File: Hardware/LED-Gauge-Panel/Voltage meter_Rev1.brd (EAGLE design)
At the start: 34.3 x 58.4 mm, 31 parts, among them J3 SL04, Q4 MOSFET-NCHANNEL2N7002PW, Q5 MOSFET-NCHANNEL2N7002PW, Q6 MOSFET-NCHANNEL2N7002PW, U1 ATMEGA328P_PDIP, U21 MAX232D, X1 22-23-2031, X2 16MHz

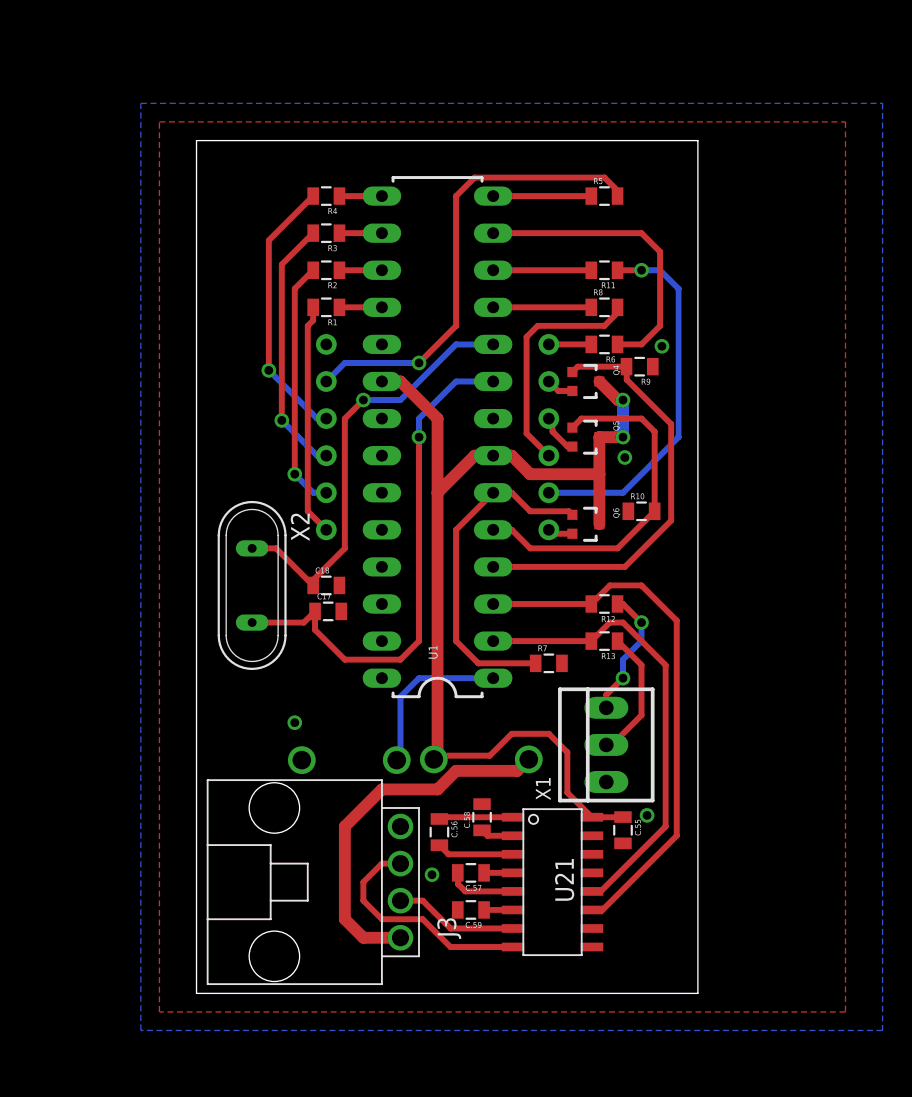
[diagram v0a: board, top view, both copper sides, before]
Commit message: Review 2 changes
Changed from n channel mosfets to p channel. Removed the resistors on
the control lines to the mosfets.
moved the resistors in series with the programming pins. And put
capacitors in the VCC lines.
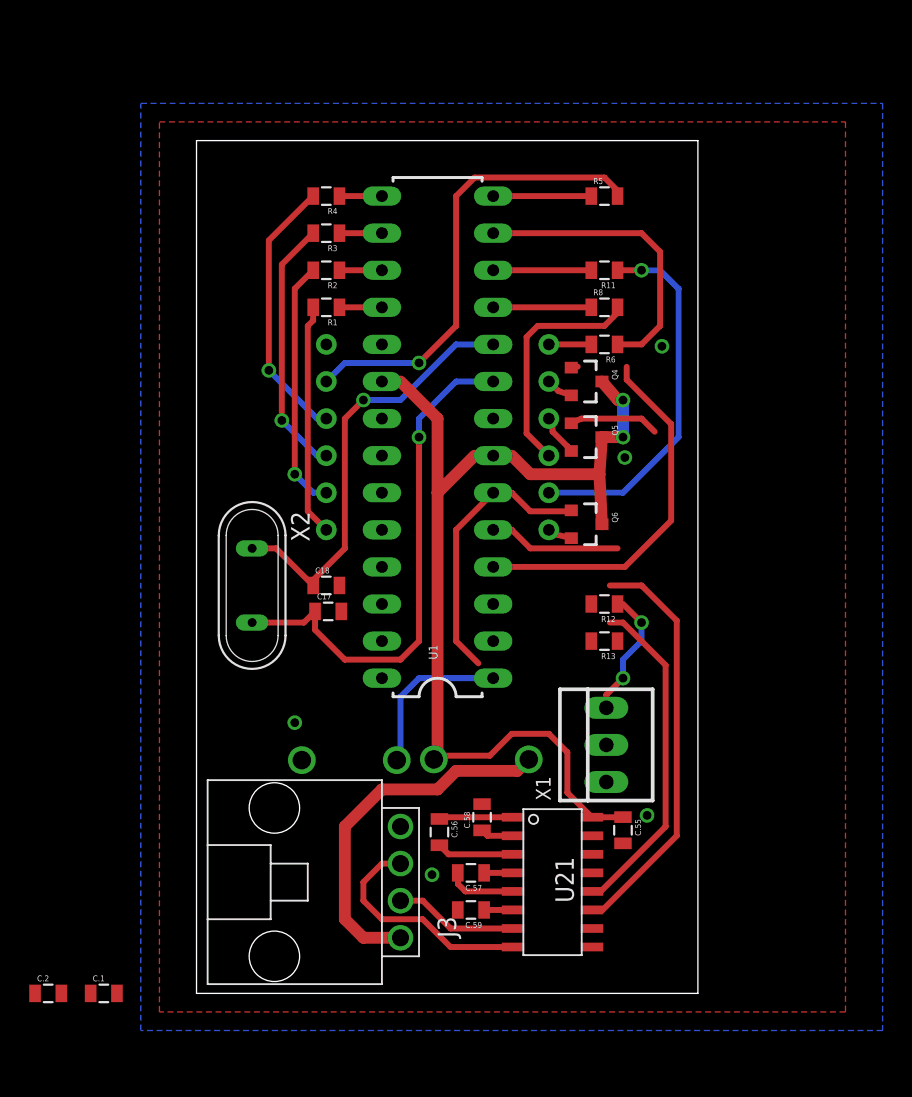
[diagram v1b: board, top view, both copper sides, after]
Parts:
- removed R10, R7, R9: 100k, SparkFun-Passives:0805
- added C.1, C.2: .1u, SparkFun-Passives:0805
- Q4, Q5, Q6: value MOSFET-NCHANNEL2N7002PW -> MOSFET-PCHANNEL; device SparkFun-DiscreteSemi:SOT323 -> SparkFun-DiscreteSemi:SOT23-3
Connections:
- new net N$15: C.2.1, U1.7
- new net N$16: C.1.1, U1.20
- net 5V: now also C.1.2, C.2.2; no longer U1.20, U1.7
- net GND: no longer R10.1, R7.2, R9.1
- net N$12: now also R13.2; no longer R13.1
- net N$14: now also R12.2; no longer R12.1
- net Q4: no longer R9.2
- net Q5: no longer R10.2
- net Q6: no longer R7.1
- net SER_RX: now also R13.1; no longer R13.2
- net SER_TX: now also R12.1; no longer R12.2
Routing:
- net Q5: track 24.4 -> 15.2 mm
- net N$12: track 9.01 -> 0.00 mm
- net SER_TX: track 36.7 -> 28.2 mm
- net SER_RX: track 31.5 -> 23.0 mm
- net 5V: track 70.5 -> 66.5 mm
- net Q6: track 23.3 -> 19.3 mm
- net Q4: track 29.2 -> 25.7 mm

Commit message: Modifications from second review
The atmega chip was changed to be surface mount. Wires were rerouted and
DRC was run. Capacitors added as well.
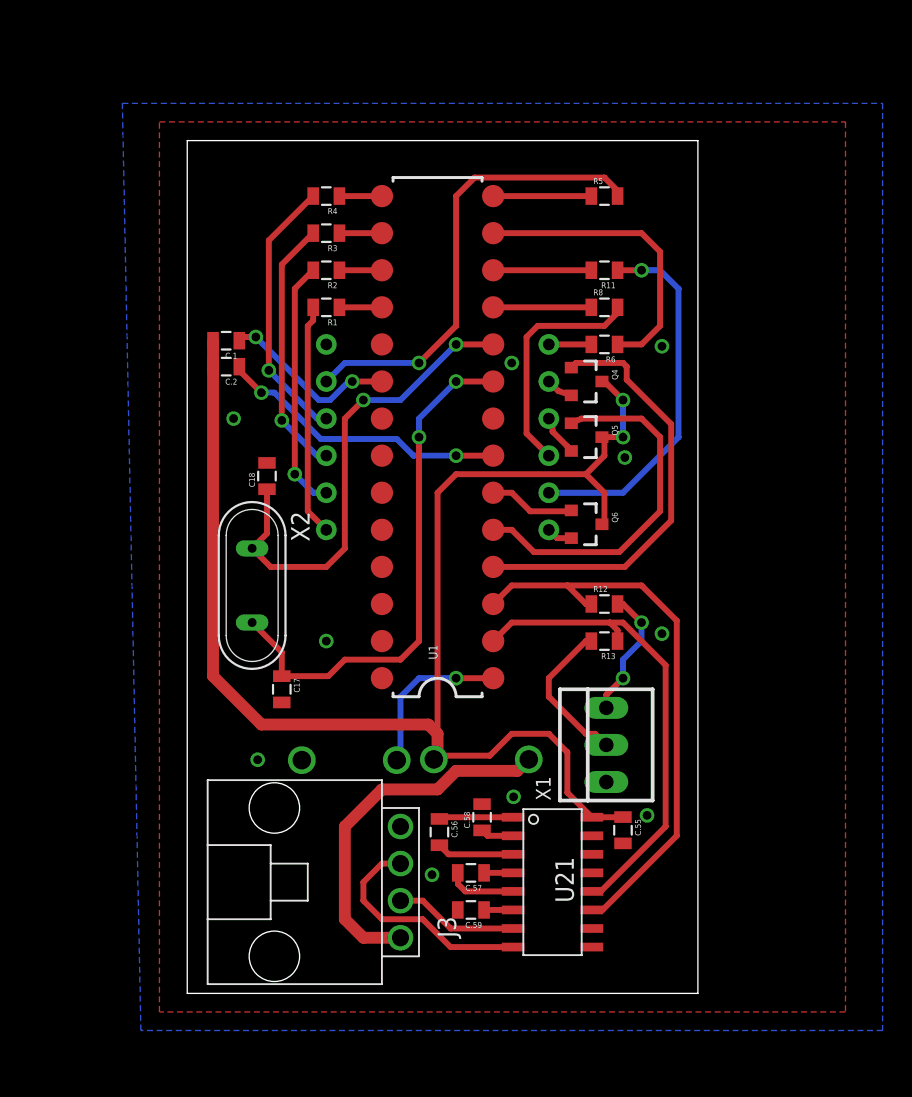
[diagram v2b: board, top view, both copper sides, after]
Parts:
- U1: value ATMEGA328P_PDIP -> ATMEGA328P_PDIPDIL28-4; device SparkFun-DigitalIC:DIL28-3 -> SparkFun-DigitalIC:CONN_IC_DIP_SOCKET_28POS
- moved C.1 45.5 mm to (4.57, 46.0), turned to 180 degrees
- moved C.2 44.6 mm to (4.57, 44.2), turned to 180 degrees
- moved C18 8.52 mm to (7.37, 36.7), turned to 90 degrees
- moved C17 6.21 mm to (8.38, 22.1), turned to 270 degrees
- moved U1 1.27 mm to (19.1, 40.6)
- turned R12 to 0 degrees
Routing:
- net 5V: track 66.5 -> 99.5 mm
- net N$15: track 0.00 -> 20.1 mm, vias 0 -> 2
- net Q6: track 19.3 -> 5.89 mm
- net N$16: track 0.00 -> 12.2 mm, vias 0 -> 2
- net SER_TX: track 28.2 -> 38.9 mm
- net N$12: track 0.00 -> 10.5 mm
- net SER_RX: track 23.0 -> 33.0 mm
- net Q5: track 15.2 -> 25.0 mm
- net Q4: track 25.7 -> 29.3 mm
- net N$51: track 29.8 -> 33.0 mm, vias 1 -> 2
- net N$50: track 35.7 -> 36.3 mm, vias 1 -> 2
- net N$13: vias 0 -> 1
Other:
- board size 34.3 x 58.4 mm -> 35 x 58.4 mm

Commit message: Reroute and label
Minor changes made to the positioning of the capacitors. Some traces
were changed due to the capacitor changes and some changes were made to
keep the trace from jumping between levels. Labels were positioned on
the board and MRDT symbol was placed on the board as well as a brief
board discription.
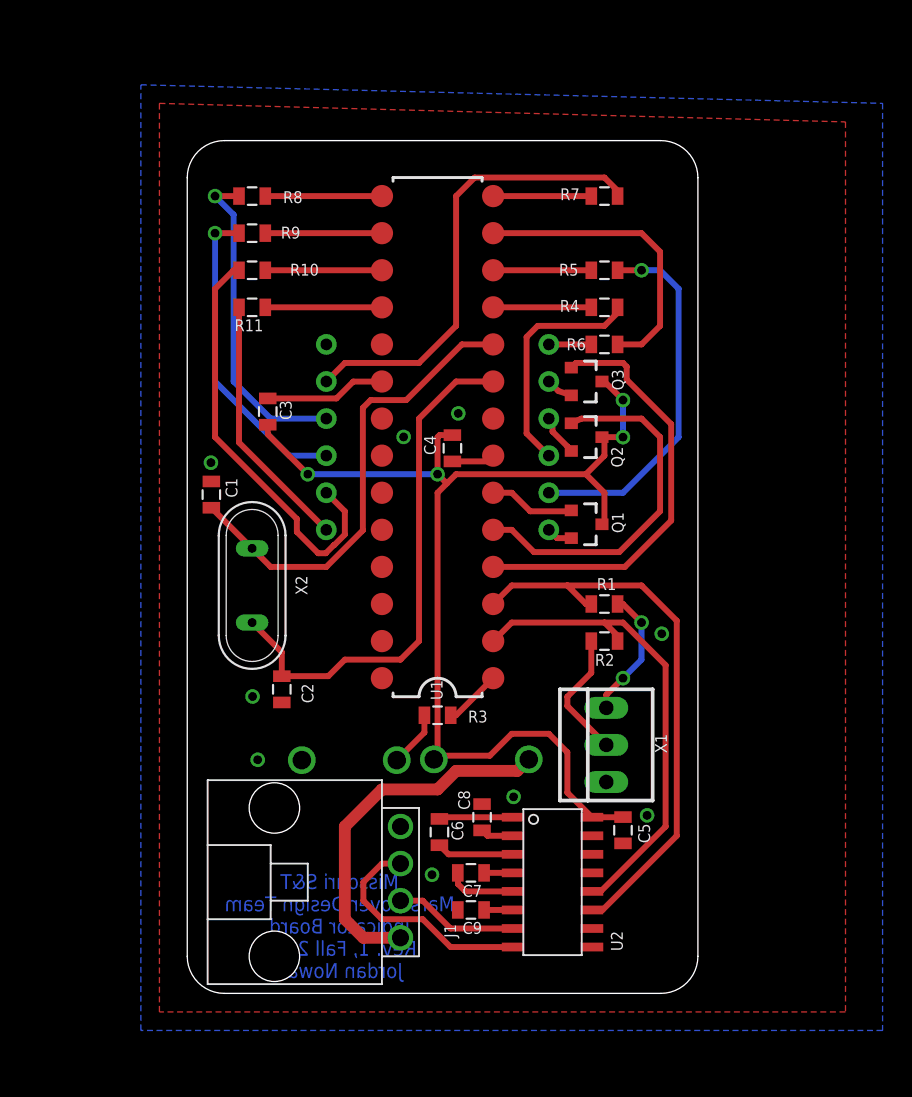
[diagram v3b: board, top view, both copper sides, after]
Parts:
- removed C.1, C.2: .1u, SparkFun-Passives:0805
- removed C18: 22pf, SparkFun-Passives:0805
- removed R12, R13: 1k, SparkFun-Passives:0805
- added C1: 22pf, SparkFun-Passives:0805
- added C3, C4: .1u, SparkFun-Passives:0805
- added LOGO1: MRDT_LOGO, MRDT-Hardware:MRDT_LOGO
- added R10, R7, R9: 330, SparkFun-Passives:0805
- R1, R2, R3: value 330 -> 1k
- moved R3 33.9 mm to (19.1, 20.3)
- moved R2 31.8 mm to (30.5, 25.4)
- moved R1 27.9 mm to (30.5, 27.9), turned to 0 degrees
- moved R8 25.3 mm to (6.35, 55.9), turned to 180 degrees
- moved R11 24.3 mm to (6.35, 48.3)
- moved R4 20.5 mm to (30.5, 48.3), turned to 0 degrees
- moved R5 5.08 mm to (30.5, 50.8), turned to 180 degrees
- moved S1 4.68 mm to (16.0, 15.5), turned to 0 degrees
- moved S2 4.68 mm to (19.1, 19.1), turned to 180 degrees
- renumbered C.55 to C5, C.56 to C6, C.57 to C7, C.58 to C8, C.59 to C9, C17 to C2, J3 to J1, Q4 to Q3, Q5 to Q2, Q6 to Q1, U21 to U2
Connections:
- new net N$24: R3.1, U1.1
- net 5V: now also C3.2, C4.2, S2.P$1; no longer C.1.2, C.2.2, S1.P$1
- net A: now also R5.1; no longer R11.1
- net C: now also R8.2; no longer R4.2
- net D: now also R10.2; no longer R2.2
- net DP: now also R9.2; no longer R3.2
- net E: now also R11.2; no longer R1.2
- net F: now also R4.2; no longer R8.2
- net G: now also R7.2; no longer R5.2
- net GND: now also C1.2, S1.P$2; no longer C18.2, S2.P$2
- net N$1: now also R7.1; no longer R5.1
- net N$10: now also R11.1; no longer R1.1
- net N$12: now also R2.2; no longer R13.2
- net N$13: now also R3.2, S1.P$1; no longer S2.P$1, U1.1
- net N$14: now also R1.2; no longer R12.2
- net N$15: now also C4.1; no longer C.2.1
- net N$16: now also C3.1; no longer C.1.1
- net N$20: now also R4.1; no longer R8.1
- net N$5: now also R8.1; no longer R4.1
- net N$51: now also C1.1; no longer C18.1
- net N$6: now also R9.1; no longer R3.1
- net N$7: now also S2.P$2; no longer S1.P$2
- net N$8: now also R5.2; no longer R11.2
- net N$9: now also R10.1; no longer R2.1
- net SER_RX: now also R2.1; no longer R13.1
- net SER_TX: now also R1.1; no longer R12.1
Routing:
- net 5V: track 99.5 -> 77.4 mm, vias 2 -> 4
- net N$15: track 20.1 -> 2.96 mm, vias 2 -> 0
- net D: track 17.2 -> 28.9 mm, vias 1 -> 0
- net N$13: track 11.3 -> 3.86 mm, vias 1 -> 0
- net N$9: track 2.91 -> 7.99 mm
- net N$6: track 2.91 -> 7.99 mm
- net N$5: track 2.91 -> 7.99 mm
- net N$10: track 2.91 -> 7.99 mm
- net N$24: track 0.00 -> 3.96 mm
- net N$16: track 12.2 -> 8.30 mm, vias 2 -> 0
- net C: track 18.5 -> 22.3 mm
- net DP: track 17.8 -> 21.5 mm
- net E: track 15.9 -> 17.7 mm
- net N$12: track 10.5 -> 8.90 mm
- net N$51: track 33.0 -> 32.2 mm, vias 2 -> 0
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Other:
- outline, holes or cut-outs redrawn
- board text added: "Missouri S&T Mars Rover Design Team Indicator Board Rev. 1, Fall 2016 Jordan Nowak"

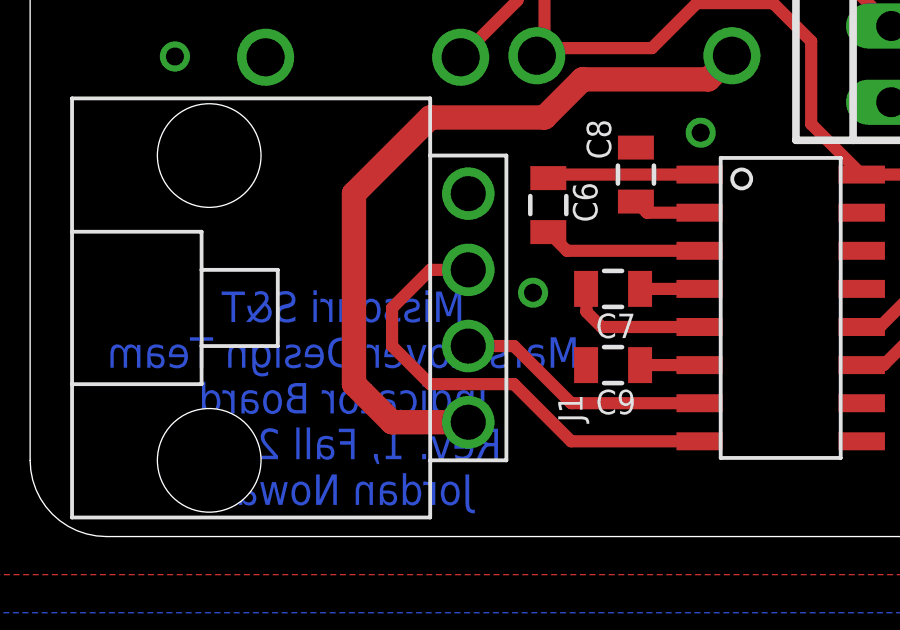
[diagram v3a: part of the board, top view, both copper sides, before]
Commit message: Updated Parts to Eagle Libraries commit 9aec81
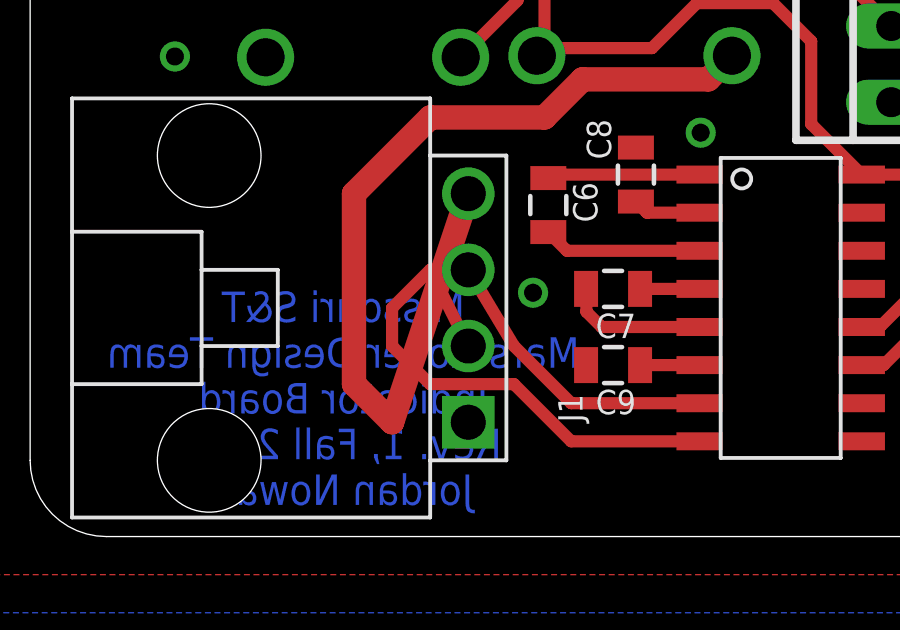
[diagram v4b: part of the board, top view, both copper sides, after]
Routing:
- net N$7: track 25.2 -> 30.7 mm
- net 232_RX: track 15.9 -> 17.5 mm
- net 232_TX: track 8.50 -> 9.94 mm
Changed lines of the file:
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@@
 <?xml version="1.0" encoding="utf-8"?>
 <!DOCTYPE eagle SYSTEM "eagle.dtd">
-<eagle version="6.5.0">
+<eagle version="7.6.0">
 <drawing>
 <settings>
@@
 <layers>
 <layer number="1" name="Top" color="4" fill="1" visible="yes" active="yes"/>
+<layer number="2" name="Route2" color="1" fill="3" visible="no" active="no"/>
+<layer number="3" name="Route3" color="4" fill="3" visible="no" active="no"/>
+<layer number="4" name="Route4" color="1" fill="4" visible="no" active="no"/>
+<layer number="5" name="Route5" color="4" fill="4" visible="no" active="no"/>
+<layer number="6" name="Route6" color="1" fill="8" visible="no" active="no"/>
+<layer number="7" name="Route7" color="4" fill="8" visible="no" active="no"/>
+<layer number="8" name="Route8" color="1" fill="2" visible="no" active="no"/>
+<layer number="9" name="Route9" color="4" fill="2" visible="no" active="no"/>
+<layer number="10" name="Route10" color="1" fill="7" visible="no" active="no"/>
+<layer number="11" name="Route11" color="4" fill="7" visible="no" active="no"/>
+<layer number="12" name="Route12" color="1" fill="5" visible="no" active="no"/>
+<layer number="13" name="Route13" color="4" fill="5" visible="no" active="no"/>
+<layer number="14" name="Route14" color="1" fill="6" visible="no" active="no"/>
+<layer number="15" name="Route15" color="4" fill="6" visible="no" active="no"/>
 <layer number="16" name="Bottom" color="1" fill="1" visible="yes" active="yes"/>
 <layer number="17" name="Pads" color="2" fill="1" visible="yes" active="yes"/>
@@
 <layer number="59" name="tCarbon" color="7" fill="1" visible="no" active="no"/>
 <layer number="60" name="bCarbon" color="7" fill="1" visible="no" active="no"/>
-<layer number="90" name="Modules" color="5" fill="1" visible="no" active="yes"/>
+<layer number="90" name="Modules" color="5" fill="1" visible="no" active="no"/>
 <layer number="91" name="Nets" color="2" fill="1" visible="no" active="no"/>
 <layer number="92" name="Busses" color="1" fill="1" visible="no" active="no"/>
@@
 <pass name="Default">
 <param name="RoutingGrid" value="50mil"/>
+<param name="AutoGrid" value="1"/>
+<param name="Efforts" value="0"/>
+<param name="TopRouterVariant" value="1"/>
 <param name="tpViaShape" value="round"/>
 <param name="PrefDir.1" value="|"/>
@@
 <wire x1="13.97" y1="7.62" x2="13.97" y2="8.89" width="0.4064" layer="1"/>
 <wire x1="13.97" y1="8.89" x2="15.24" y2="10.16" width="0.4064" layer="1"/>
-<wire x1="15.24" y1="10.16" x2="16.51" y2="10.16" width="0.4064" layer="1"/>
+<wire x1="15.24" y1="10.16" x2="16.51" y2="7.62" width="0.4064" layer="1"/>
 </signal>
 <signal name="232_TX">
@@
 <wire x1="24.224" y1="5.715" x2="19.939" y2="5.715" width="0.4064" layer="1"/>
 <wire x1="19.939" y1="5.715" x2="18.034" y2="7.62" width="0.4064" layer="1"/>
-<wire x1="18.034" y1="7.62" x2="16.51" y2="7.62" width="0.4064" layer="1"/>
+<wire x1="18.034" y1="7.62" x2="16.51" y2="10.16" width="0.4064" layer="1"/>
 </signal>
 <signal name="SER_RX">
@@
 <wire x1="12.7" y1="12.7" x2="12.7" y2="6.35" width="0.8128" layer="1"/>
 <wire x1="12.7" y1="6.35" x2="13.97" y2="5.08" width="0.8128" layer="1"/>
-<wire x1="13.97" y1="5.08" x2="16.51" y2="5.08" width="0.8128" layer="1"/>
+<wire x1="13.97" y1="5.08" x2="16.51" y2="12.7" width="0.8128" layer="1"/>
 </signal>
 <signal name="5V">
